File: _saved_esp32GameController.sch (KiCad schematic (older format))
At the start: 25 parts, among them IC1 BQ21040DBVT, IC2 ESP-WROOM-32_(16MB), J1 USB_B_Micro, J2 Conn_01x02_Male, J3 Conn_02x06_Odd_Even, Q1 2N2219, Q2 2N2219, U1 WIICHUCK, U2 TPS62202DBV

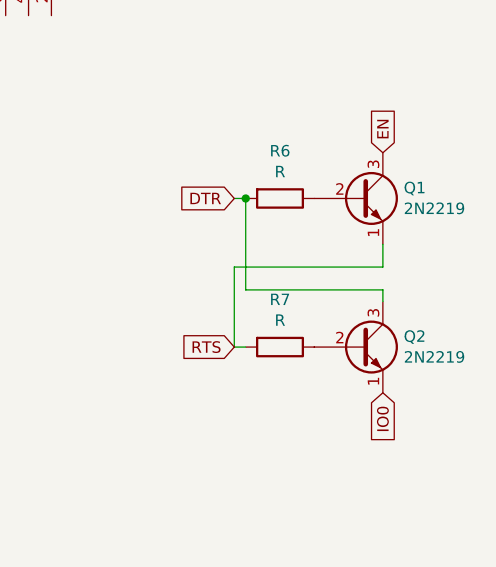
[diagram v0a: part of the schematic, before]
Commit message: Updated footprint and pinouts
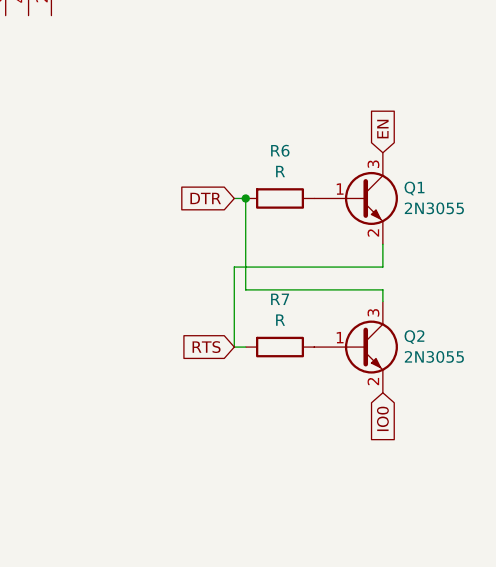
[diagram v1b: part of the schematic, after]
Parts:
- removed Q1, Q2: 2N2219, Package_TO_SOT_SMD:SOT-23, symbol Transistor_BJT:2N2219
- added Q1, Q2: 2N3055, Package_TO_SOT_SMD:SOT-23, symbol Transistor_BJT:2N3055
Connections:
- net DTR: now also Q2.3 (C)
- net EN: now also Q1.3 (C)
- net IO0: now also Q2.2 (E)
- net RTS: now also Q1.2 (E)
- net at R6.1: now also Q1.1 (B)
- net at R7.1: now also Q2.1 (B)
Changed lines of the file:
@@
 EESchema Schematic File Version 4
+LIBS:esp32GameController-cache
 EELAYER 26 0
 EELAYER END
@@
 Connection ~ 5800 2250
 $Comp
-L Transistor_BJT:2N2219 Q2
-U 1 1 5C8E7434
-P 10650 2950
-F 0 "Q2" H 10841 2996 50  0000 L CNN
-F 1 "2N2219" H 10841 2905 50  0000 L CNN
-F 2 "Package_TO_SOT_SMD:SOT-23" H 10850 2875 50  0001 L CIN
-F 3 "http://www.onsemi.com/pub_link/Collateral/2N2219-D.PDF" H 10650 2950 50  0001 L CNN
-	1    10650 2950
-	1    0    0    -1
-$EndComp
-$Comp
 L Connector_Generic:Conn_02x06_Odd_Even J3
 U 1 1 5C8E861B
@@
 	10750 2700 10750 2750
 Connection ~ 10150 2300
-$Comp
-L Transistor_BJT:2N2219 Q1
-U 1 1 5C8E73F2
-P 10650 2300
-F 0 "Q1" H 10841 2346 50  0000 L CNN
-F 1 "2N2219" H 10841 2255 50  0000 L CNN
-F 2 "Package_TO_SOT_SMD:SOT-23" H 10850 2225 50  0001 L CIN
-F 3 "http://www.onsemi.com/pub_link/Collateral/2N2219-D.PDF" H 10650 2300 50  0001 L CNN
-	1    10650 2300
-	1    0    0    -1
-$EndComp
-Wire Wire Line
-	10750 2600 10750 2500
 Wire Wire Line
 	10100 2600 10750 2600
@@
 Text GLabel 7750 2550 2    50   Input ~ 0
 IO0
+Wire Wire Line
+	10750 2500 10750 2600
+$Comp
+L Transistor_BJT:2N3055 Q1
+U 1 1 5C8FA7AB
+P 10650 2300
+F 0 "Q1" H 10841 2346 50  0000 L CNN
+F 1 "2N3055" H 10841 2255 50  0000 L CNN
+F 2 "Package_TO_SOT_SMD:SOT-23" H 10850 2225 50  0001 L CIN
+F 3 "http://www.onsemi.com/pub_link/Collateral/2N3055-D.PDF" H 10650 2300 50  0001 L CNN
+	1    10650 2300
+	1    0    0    -1
+$EndComp
+$Comp
+L Transistor_BJT:2N3055 Q2
+U 1 1 5C8FB335
+P 10650 2950
+F 0 "Q2" H 10841 2996 50  0000 L CNN
+F 1 "2N3055" H 10841 2905 50  0000 L CNN
+F 2 "Package_TO_SOT_SMD:SOT-23" H 10850 2875 50  0001 L CIN
+F 3 "http://www.onsemi.com/pub_link/Collateral/2N3055-D.PDF" H 10650 2950 50  0001 L CNN
+	1    10650 2950
+	1    0    0    -1
+$EndComp
 $EndSCHEMATC
